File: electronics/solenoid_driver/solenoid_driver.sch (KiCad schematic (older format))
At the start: 7 parts

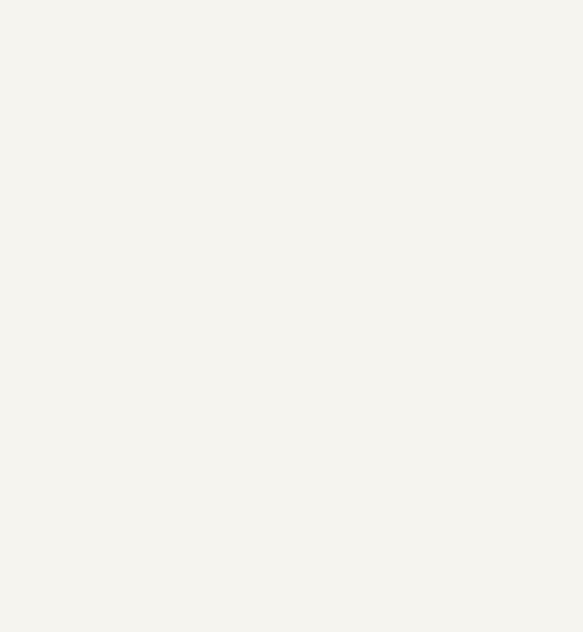
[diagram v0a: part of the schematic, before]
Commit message: Move shift registers to solenoid driver
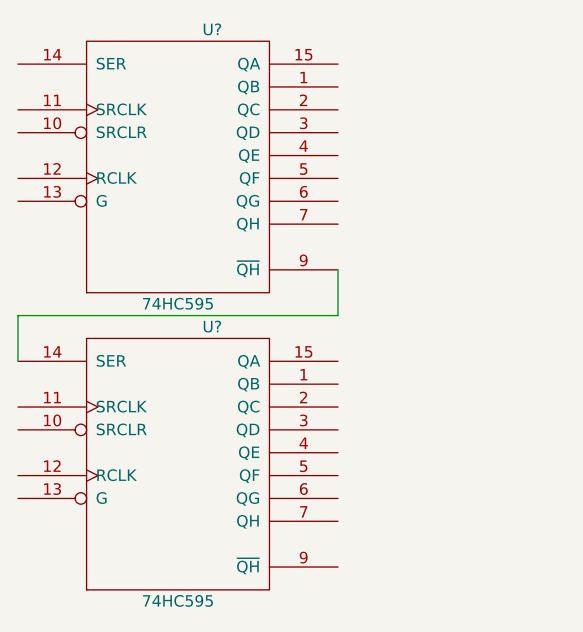
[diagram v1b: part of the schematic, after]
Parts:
- added U? (x2): 74HC595, symbol 74HC595
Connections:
- wire segments 11 -> 14
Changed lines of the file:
@@
 Wire Wire Line
 	6200 4200 6200 4100
+$Comp
+L 74HC595 U?
+U 1 1 56DE4E3F
+P 3800 2850
+F 0 "U?" H 3950 3450 50  0000 C CNN
+F 1 "74HC595" H 3800 2250 50  0000 C CNN
+F 2 "" H 3800 2850 50  0000 C CNN
+F 3 "" H 3800 2850 50  0000 C CNN
+	1    3800 2850
+	1    0    0    -1
+$EndComp
+$Comp
+L 74HC595 U?
+U 1 1 56DE4E6E
+P 3800 4150
+F 0 "U?" H 3950 4750 50  0000 C CNN
+F 1 "74HC595" H 3800 3550 50  0000 C CNN
+F 2 "" H 3800 4150 50  0000 C CNN
+F 3 "" H 3800 4150 50  0000 C CNN
+	1    3800 4150
+	1    0    0    -1
+$EndComp
+Wire Wire Line
+	4500 3300 4500 3500
+Wire Wire Line
+	4500 3500 3100 3500
+Wire Wire Line
+	3100 3500 3100 3700
 $EndSCHEMATC

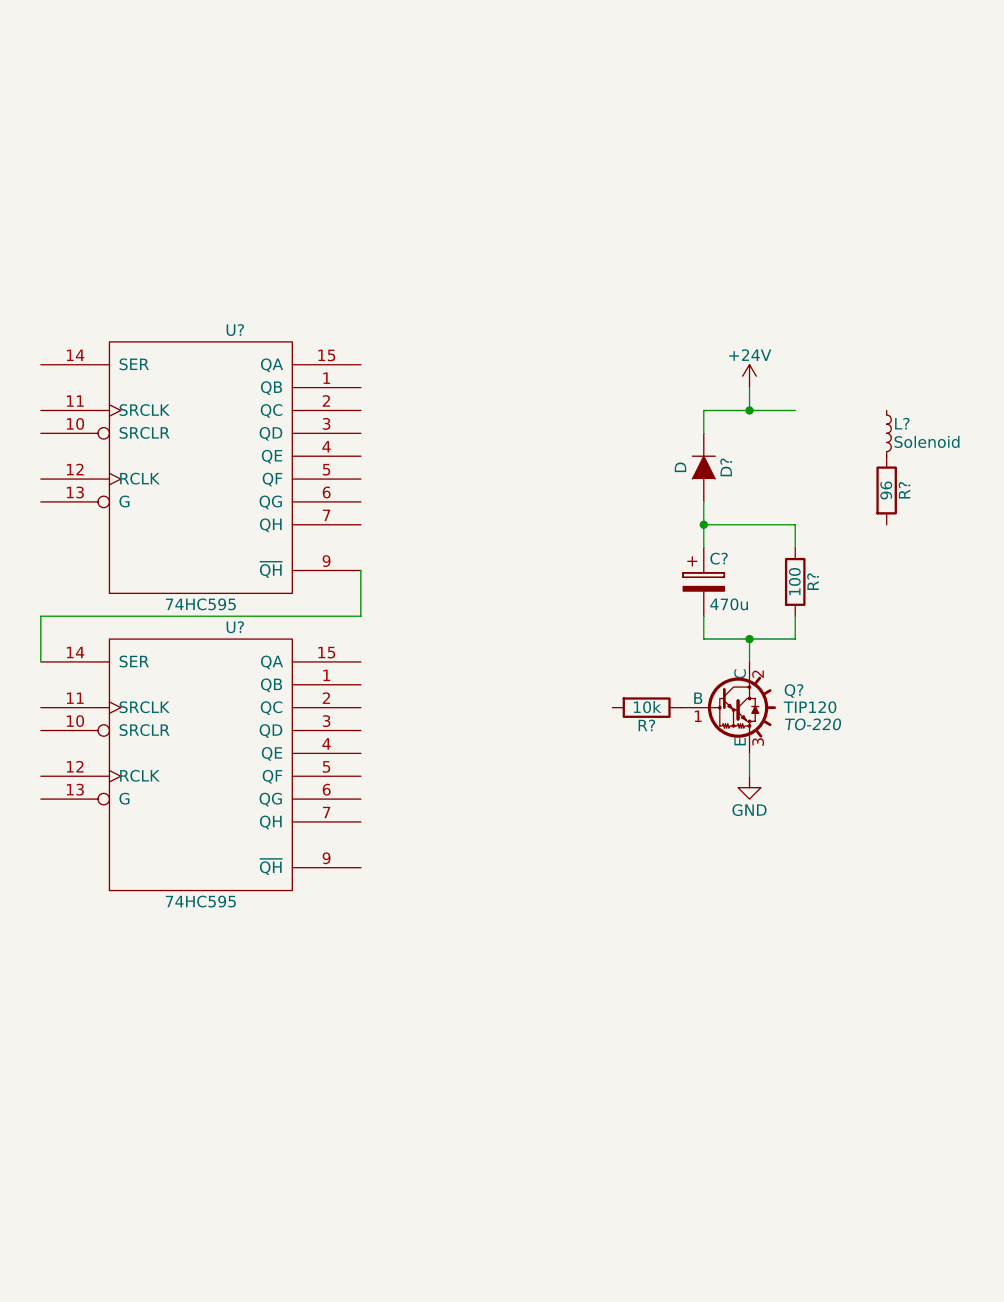
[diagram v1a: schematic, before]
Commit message: Add sub sheet for BJT driver
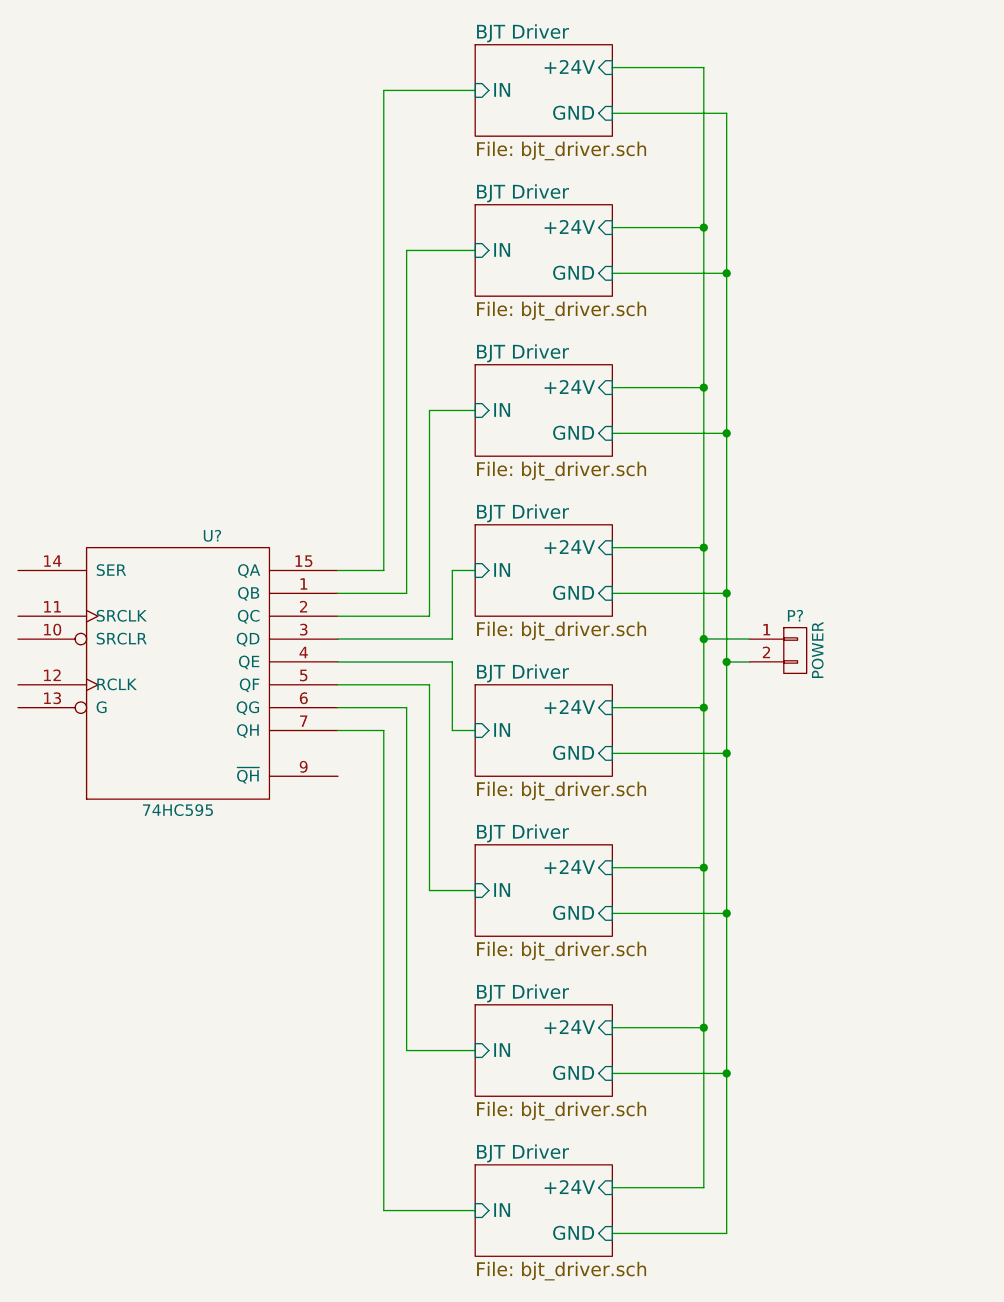
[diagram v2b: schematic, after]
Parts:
- removed C?: 470u, symbol CP
- removed D?: D, symbol D
- removed L?: Solenoid, symbol L_Small
- removed Q?: TIP120, TO-220, symbol TIP120
- removed R?: 10k, symbol R
- removed R?: 100, symbol R
- removed R?: 96, symbol R
- removed U?: 74HC595, symbol 74HC595
- added P?: POWER, symbol CONN_01X02
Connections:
- net labels removed: +24V, GND
- wire segments 14 -> 44
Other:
- moved on the sheet: U?
